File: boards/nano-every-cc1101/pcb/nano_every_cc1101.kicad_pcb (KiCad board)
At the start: 2 copper layers, 70 x 45 mm, 74 parts, among them J1 SMA, J2 SMA, J3 Breakout 1-15, J4 Breakout 16-30, U1 CC1101RGPR, U2 XC6206P332MR, U3 TXS0108EPWR, U501 CC1101RGPR, Y1 26MHz, Y501 26MHz

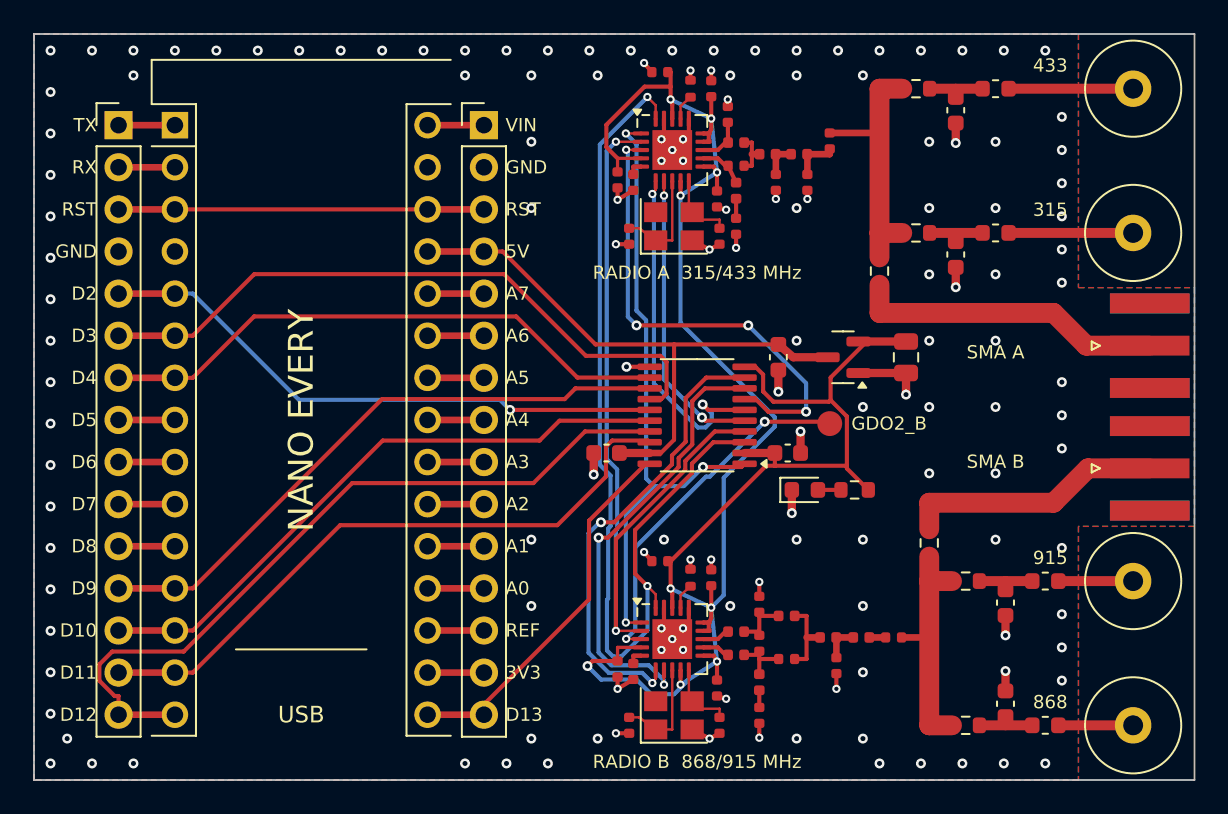
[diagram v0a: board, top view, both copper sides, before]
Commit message: nano-every-cc1101: pre-order verification, shorter routing, JLCPCB-exact CPL
Checks (verify/, re-run with verify/run_all.sh, report in VERIFICATION.md):
- DRC 0/0; Gerber DFM on the fab zip against JLCPCB 2-layer limits
- every IC pin vs the vendor (JLCPCB/EasyEDA) pin names, Nano vs ABX00028
- CPL: JLCPCB's own footprint of each part fitted onto the board pads;
  all 66 parts match. Fixes U3 (TSSOP), U2 (SOT-23, would have been
  reversed), J3/J4 and S1/S2 angles, now applied in fab_outputs.py
- live stock for 5 boards; decoupling distances; crystal load
- 2-D field solver for the CPWG lines (1.2 mm/0.2 mm = 49.7-51.4 ohm)
- nodal simulation of both antenna feeds from the routed copper
  (S11 -19..-35 dB, 97-99 % to the coil); CC1101 harmonic filters; power

Changes:
- TXS0108E at 270 deg, channels in Nano pin order (shortest of 24 routed
  placements): 622 mm autorouted / 9 vias (was 661 / 11); same Nano pins
- silkscreen to JLCPCB minimums (1.0 mm text, 0.15 mm strokes, 0.15 mm
  from pads); clean ABX00028 outline; vias kept off the pin labels
- coil branches 50 ohm (1.2 mm) end to end; zero-length router stubs removed
- docs: Economic PCBA (board < 70 x 70 mm), verification section

Co-Authored-By: Claude Opus 5.5 <noreply@anthropic.com>
Claude-Session: https://claude.ai/code/session_019aUkwoH7eUuCGWSrK9KSBc
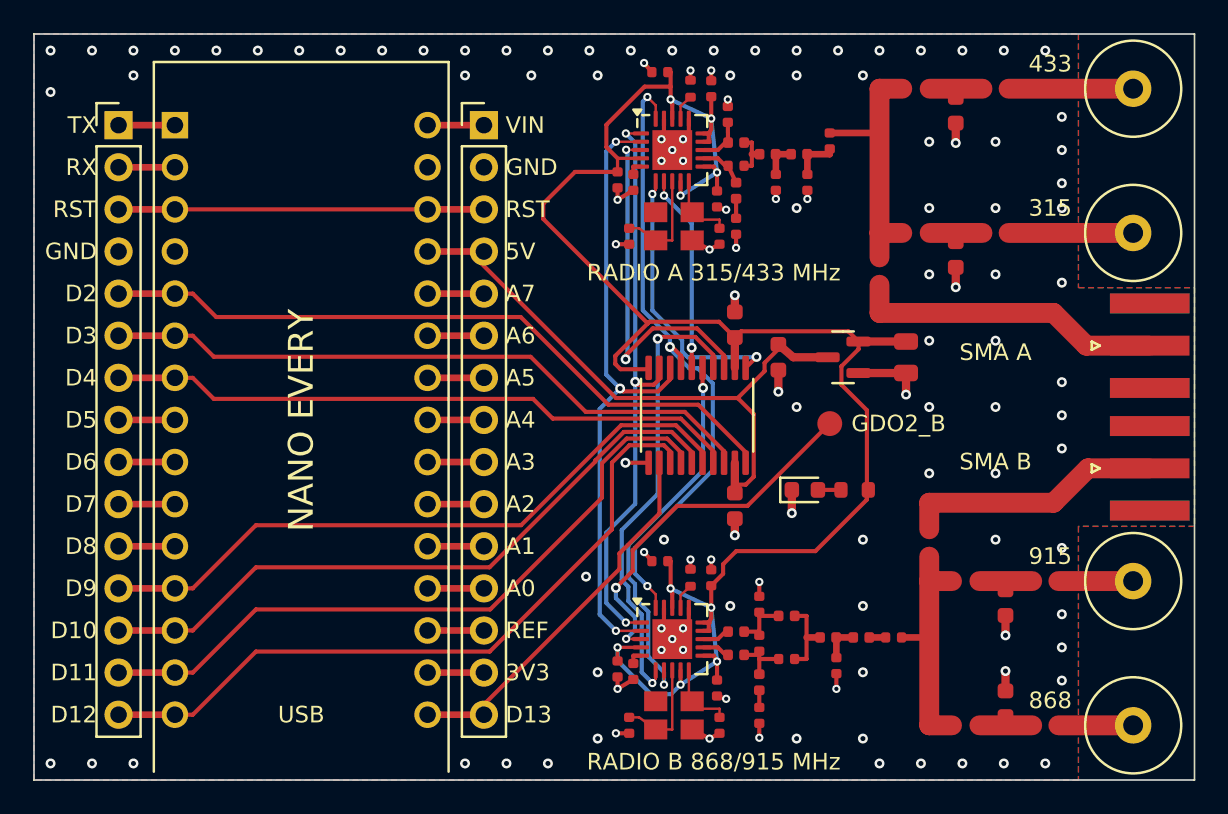
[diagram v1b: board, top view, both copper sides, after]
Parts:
- moved C7 8.37 mm to (142.3, 117.5), turned to 90 degrees
- moved C8 8.37 mm to (142.3, 128.5), turned to 90 degrees
- turned U3 to -90 degrees
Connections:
- U3 pad 1: SCLK -> GDO0_A
- U3 pad 12: D4 -> D13_SCK
- U3 pad 13: D9 -> D12_MISO
- U3 pad 14: D3 -> D11_MOSI
- U3 pad 15: D2 -> D10
- U3 pad 16: D10 -> D9
- U3 pad 17: D12_MISO -> D4
- U3 pad 18: D11_MOSI -> D3
- U3 pad 20: D13_SCK -> D2
- U3 pad 3: SI -> GDO2_A
- U3 pad 4: SO -> GDO0_B
- U3 pad 5: CSN_A -> CSN_B
- U3 pad 6: GDO0_A -> CSN_A
- U3 pad 7: GDO2_A -> SI
- U3 pad 8: CSN_B -> SO
- U3 pad 9: GDO0_B -> SCLK
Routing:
- net SI: track 56.7 -> 38.6 mm, vias 2 -> 3
- net SO: track 49.3 -> 38.1 mm, vias 2 -> 3
- net D2: track 34.9 -> 42.4 mm, vias 1 -> 0
- net GDO2_A: track 29.6 -> 22.3 mm, vias 4 -> 2
- net 3V3: track 121.4 -> 115.1 mm
- net CSN_A: track 17.8 -> 11.9 mm
- net CSN_B: track 27.1 -> 22.7 mm
- net GDO0_A: track 21.0 -> 16.7 mm
- net SCLK: track 38.8 -> 35.1 mm
- net D9: track 37.0 -> 40.6 mm
- net D10: track 37.3 -> 40.7 mm
- net D4: track 35.1 -> 38.4 mm
- net D11_MOSI: track 38.9 -> 42.0 mm
- net D12_MISO: track 46.1 -> 43.2 mm
- net +5V: track 36.1 -> 38.9 mm
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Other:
- board text added: "70 x 45 mm 2-layer v2.1"
- board text added: "A: 433 R301 315 R311 SMA R403"
- board text added: "ANTENNA: fit ONE selector/radio"
- board text added: "B: 868 R321 915 R331 SMA R406"
- board text added: "SPI D13 SCK D11 MOSI D12 MISO"
- board text added: "coil retune: C3x1 shunt, L3x1"
- board text removed: "2-layer 70 x 45 mm v2.0 coil antennas"
- board text removed: "A: 433 coil R301 | 315 coil R311 | SMA R403"
- board text removed: "ANTENNA - fit ONE selector per radio"
- board text removed: "B: 868 coil R321 | 915 coil R331 | SMA R406"
- board text removed: "SPI: D13 SCK D11 MOSI D12 MISO"
- board text removed: "coil retune: C3x1 shunt, L3x1 series"

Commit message: nano-every-cc1101 v2.2: deeper pre-order recheck and fixes
New independent checks (verify/): netlist rebuilt from the Gerber and drill
files alone (0 shorts, 0 opens, all 73 nets) with JLCPCB's copper, drill,
annular-ring, mask and paste limits measured on them; every SMD pair against
JLCPCB's spacing table; every BOM line against its live LCSC record; firmware
pins traced through the board; a 3-D openEMS simulation of the 50 ohm line
(51.8 ohm vs 52.2 ohm from the 2-D solver for the same geometry).

Fixes from what they found:
- Coils: the bent-leg spring antennas lie in the board plane beyond an edge
  (makers' drawings, JLCPCB 3D models), not upright. New edge-overhang
  footprints, hole 2 mm from the right edge, CPL angles fitted to JLCPCB's
  outlines so every coil points off the edge.
- Radio B coils now Vollgo VG868SNX18-5W2 / VG915SNX17-5W2 (maker-measured
  VSWR 1.32 / 1.56 vs 5.3 / 2.6 for the BAT WIRELESS parts).
- CC1101 exposed pad: vias tented on the component side per TI, paste and
  mask only in four windows between them.
- DCOUPL cap C51/C551 0.3 mm clear of the QFN with a 0.22 mm mask web;
  ground vias kept outside their pads' mask openings (0 exposed vias).
- 12 nH balun inductor: LQW15AN12NG00D (C86128) in place of the low-stock
  LQW15AN12NJ00D.
- Coil holes sized for the wire (1.0 / 1.1 mm).
- Level shifter placement searched again: 644 mm autorouted, 11 vias.
- Example sketch: 135 kHz RX filter for +/-10 ppm crystals.
- Docs, BOMs, CPL, Gerbers, renders and VERIFICATION.md regenerated.

Co-Authored-By: Claude Opus 5.5 <noreply@anthropic.com>
Claude-Session: https://claude.ai/code/session_019aUkwoH7eUuCGWSrK9KSBc
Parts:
- AE1: footprint nano_every_cc1101:Coil_Spring_D5.5_THT -> nano_every_cc1101:Coil_BW433SNX21-5W2_EdgeOverhang
- AE2: footprint nano_every_cc1101:Coil_Spring_D5.5_THT -> nano_every_cc1101:Coil_BW315SNX39-6W3_EdgeOverhang
- AE3: value BW868SNX20-5Z6 -> VG868SNX18-5W2; footprint nano_every_cc1101:Coil_Spring_D5.5_THT -> nano_every_cc1101:Coil_VG868SNX18-5W2_EdgeOverhang
- AE4: value BW915SNX17-5W2 -> VG915SNX17-5W2; footprint nano_every_cc1101:Coil_Spring_D5.5_THT -> nano_every_cc1101:Coil_VG915SNX17-5W2_EdgeOverhang
- moved AE2 1.77 mm to (168.0, 111.5)
- moved AE1 1.70 mm to (168.0, 103.3)
- moved AE3 1.70 mm to (168.0, 141.7)
- moved AE4 1.70 mm to (168.0, 133.0)
- moved C311 0.50 mm to (155.6, 112.8)
- moved L311 0.50 mm to (158.0, 111.5)
- moved R311 0.50 mm to (153.2, 111.5)
- moved R403 0.50 mm to (151.0, 113.8)
- moved C551 0.25 mm to (135.9, 138.6)
- moved C51 0.25 mm to (135.9, 109.1)
- moved C111 0.20 mm to (141.0, 110.0)
- moved C41 0.20 mm to (135.0, 108.8)
- moved C541 0.20 mm to (135.0, 138.3)
- moved C611 0.20 mm to (141.0, 139.4)
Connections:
- U3 pad 1: GDO0_A -> SCLK
- U3 pad 12: D13_SCK -> D2
- U3 pad 13: D12_MISO -> D3
- U3 pad 14: D11_MOSI -> D4
- U3 pad 15: D10 -> D9
- U3 pad 16: D9 -> D10
- U3 pad 17: D4 -> D11_MOSI
- U3 pad 18: D3 -> D12_MISO
- U3 pad 20: D2 -> D13_SCK
- U3 pad 3: GDO2_A -> SO
- U3 pad 4: GDO0_B -> SI
- U3 pad 5: CSN_B -> CSN_A
- U3 pad 6: CSN_A -> CSN_B
- U3 pad 7: SI -> GDO0_B
- U3 pad 8: SO -> GDO2_A
- U3 pad 9: SCLK -> GDO0_A
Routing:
- net SI: track 38.6 -> 53.0 mm, vias 3 -> 4
- net GDO2_B: track 22.9 -> 30.0 mm
- net GDO2_A: track 22.3 -> 16.8 mm
- net GDO0_B: track 27.9 -> 33.3 mm
- net SCLK: track 35.1 -> 40.4 mm
- net D13_SCK: track 23.2 -> 28.5 mm
- net GDO0_A: track 16.7 -> 11.5 mm
- net D2: track 42.4 -> 37.5 mm
- net SO: track 38.1 -> 42.0 mm
- net 3V3: track 115.1 -> 118.6 mm, vias 9 -> 8
- net D9: track 40.6 -> 38.1 mm
- net D3: track 40.1 -> 38.4 mm
- net FEED_915: track 4.51 -> 6.21 mm
- net FEED_868: track 4.51 -> 6.21 mm
- net FEED_433: track 7.51 -> 9.21 mm
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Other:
- board text added: "70 x 45 mm 2-layer v2.2"
- board text removed: "70 x 45 mm 2-layer v2.1"
